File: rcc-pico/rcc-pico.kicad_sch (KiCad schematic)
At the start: 51 parts, among them J1 Conn_02x02_Odd_Even, J10 Conn_02x04_Odd_Even, J11 Conn_02x04_Odd_Even, J12 Conn_02x04_Odd_Even, J14 Conn_02x05_Odd_Even, J16 Conn_01x02_Pin, J3 PJ-006A, J5 Conn_3x4_female, J7 Conn_03x10, J8 Screw_Terminal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

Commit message: fixed D2 footprint
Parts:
- D2: footprint LED_SMD:LED_0603_1608Metric_Pad1.05x0.95mm_HandSolder -> LED_SMD:LED_0603_1608Metric
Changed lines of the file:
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@@
       (effects (font (size 1.27 1.27)))
     )
-    (property "Footprint" "LED_SMD:LED_0603_1608Metric_Pad1.05x0.95mm_HandSolder" (at 60.96 124.46 0)
+    (property "Footprint" "LED_SMD:LED_0603_1608Metric" (at 60.96 124.46 0)
       (effects (font (size 1.27 1.27)) hide)
     )

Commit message: final touches, fixed footprints
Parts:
- R10, R5, R6, R7, R8, R9: footprint Resistor_SMD:R_0603_1608Metric_Pad0.98x0.95mm_HandSolder -> Resistor_SMD:R_0603_1608Metric
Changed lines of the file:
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@@
       (effects (font (size 1.27 1.27)) (justify left))
     )
-    (property "Footprint" "Resistor_SMD:R_0603_1608Metric_Pad0.98x0.95mm_HandSolder" (at 94.996 170.434 90)
+    (property "Footprint" "Resistor_SMD:R_0603_1608Metric" (at 94.996 170.434 90)
       (effects (font (size 1.27 1.27)) hide)
     )
@@
       (effects (font (size 1.27 1.27)) (justify left))
     )
-    (property "Footprint" "Resistor_SMD:R_0603_1608Metric_Pad0.98x0.95mm_HandSolder" (at 65.786 170.434 90)
+    (property "Footprint" "Resistor_SMD:R_0603_1608Metric" (at 65.786 170.434 90)
       (effects (font (size 1.27 1.27)) hide)
     )
@@
       (effects (font (size 1.27 1.27)) (justify left))
     )
-    (property "Footprint" "Resistor_SMD:R_0603_1608Metric_Pad0.98x0.95mm_HandSolder" (at 50.546 170.434 90)
+    (property "Footprint" "Resistor_SMD:R_0603_1608Metric" (at 50.546 170.434 90)
       (effects (font (size 1.27 1.27)) hide)
     )
@@
       (effects (font (size 1.27 1.27)) (justify left))
     )
-    (property "Footprint" "Resistor_SMD:R_0603_1608Metric_Pad0.98x0.95mm_HandSolder" (at 36.576 170.434 90)
+    (property "Footprint" "Resistor_SMD:R_0603_1608Metric" (at 36.576 170.434 90)
       (effects (font (size 1.27 1.27)) hide)
     )
@@
       (effects (font (size 1.27 1.27)) (justify left))
     )
-    (property "Footprint" "Resistor_SMD:R_0603_1608Metric_Pad0.98x0.95mm_HandSolder" (at 21.336 170.434 90)
+    (property "Footprint" "Resistor_SMD:R_0603_1608Metric" (at 21.336 170.434 90)
       (effects (font (size 1.27 1.27)) hide)
     )
@@
       (effects (font (size 1.27 1.27)) (justify left))
     )
-    (property "Footprint" "Resistor_SMD:R_0603_1608Metric_Pad0.98x0.95mm_HandSolder" (at 79.756 170.434 90)
-      (effects (font (size 1.27 1.27)) hide)
-    )
+    (property "Footprint" "Resistor_SMD:R_0603_1608Metric" (at 79.756 170.434 90)
+      (effects (font (size 1.27 1.27)) hide)
+    )

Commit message: changed 0.1uH footprint, added v0.2 BOM
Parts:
- C1, C7: footprint Capacitor_SMD:C_0603_1608Metric -> Capacitor_SMD:C_0402_1005Metric
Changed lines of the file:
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@@
       (effects (font (size 1.27 1.27)))
     )
-    (property "Footprint" "Capacitor_SMD:C_0603_1608Metric" (at 138.43 32.0548 0)
+    (property "Footprint" "Capacitor_SMD:C_0402_1005Metric" (at 138.43 32.0548 0)
       (effects (font (size 1.27 1.27)) hide)
     )
@@
       (effects (font (size 1.27 1.27)))
     )
-    (property "Footprint" "Capacitor_SMD:C_0603_1608Metric" (at 210.5152 78.74 0)
+    (property "Footprint" "Capacitor_SMD:C_0402_1005Metric" (at 210.5152 78.74 0)
       (effects (font (size 1.27 1.27)) hide)
     )

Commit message: ordering v0.2
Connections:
- net GND: no longer H1.1, H2.1, H3.1, H4.1
- net GPIO26: now also J4.25 (5); no longer J4.3 (Pin_3)
- net GPIO27: now also J4.26 (6); no longer J4.25 (5)
- net GPIO28: now also J4.3 (Pin_3); no longer J4.26 (6)
- no-connect marks 16 -> 20
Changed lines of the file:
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@@
   (no_connect (at 256.54 22.86))
   (no_connect (at 276.86 20.32))
+  (no_connect (at 191.77 48.26))
   (no_connect (at 203.2 86.36))
   (no_connect (at 276.86 22.86))
@@
   (no_connect (at 243.84 22.86))
   (no_connect (at 187.96 132.08))
+  (no_connect (at 191.77 31.75))
   (no_connect (at 264.16 22.86))
+  (no_connect (at 191.77 39.37))
   (no_connect (at 203.2 78.74))
   (no_connect (at 203.2 88.9))
   (no_connect (at 276.86 25.4))
   (no_connect (at 264.16 20.32))
+  (no_connect (at 191.77 55.88))
   (no_connect (at 182.88 132.08))
   (wire (pts (xy 30.48 43.18) (xy 33.02 43.18))
@@
     (effects (font (size 1.27 1.27)) (justify right bottom))
   )
+  (label "GPIO28" (at 234.95 78.74 0) (fields_autoplaced)
+    (effects (font (size 1.27 1.27)) (justify left bottom))
+  )
   (label "GPIO27" (at 203.2 99.06 0) (fields_autoplaced)
     (effects (font (size 1.27 1.27)) (justify left bottom))
@@
     (effects (font (size 1.27 1.27)) (justify right bottom))
   )
+  (label "GPIO26" (at 254 83.82 0) (fields_autoplaced)
+    (effects (font (size 1.27 1.27)) (justify left bottom))
+  )
   (label "GND" (at 167.64 121.92 180) (fields_autoplaced)
     (effects (font (size 1.27 1.27)) (justify right bottom))
@@
     (effects (font (size 1.27 1.27)) (justify right bottom))
   )
-  (label "GND" (at 191.77 48.26 0) (fields_autoplaced)
-    (effects (font (size 1.27 1.27)) (justify left bottom))
-  )
   (label "GPIO10" (at 130.81 113.03 180) (fields_autoplaced)
     (effects (font (size 1.27 1.27)) (justify right bottom))
   )
-  (label "GND" (at 191.77 31.75 0) (fields_autoplaced)
-    (effects (font (size 1.27 1.27)) (justify left bottom))
-  )
   (label "GND" (at 203.2 83.82 0) (fields_autoplaced)
     (effects (font (size 1.27 1.27)) (justify left bottom))
@@
     (effects (font (size 1.27 1.27)) (justify right bottom))
   )
-  (label "GPIO27" (at 254 83.82 0) (fields_autoplaced)
-    (effects (font (size 1.27 1.27)) (justify left bottom))
-  )
   (label "GPIO14" (at 167.64 124.46 180) (fields_autoplaced)
     (effects (font (size 1.27 1.27)) (justify right bottom))
@@
     (effects (font (size 1.27 1.27)) (justify right bottom))
   )
-  (label "GND" (at 191.77 55.88 0) (fields_autoplaced)
-    (effects (font (size 1.27 1.27)) (justify left bottom))
-  )
-  (label "GPIO28" (at 254 86.36 0) (fields_autoplaced)
-    (effects (font (size 1.27 1.27)) (justify left bottom))
-  )
   (label "adcref_3v3" (at 265.43 54.61 0) (fields_autoplaced)
     (effects (font (size 1.27 1.27)) (justify left bottom))
@@
     (effects (font (size 1.27 1.27)) (justify left bottom))
   )
-  (label "GND" (at 191.77 39.37 0) (fields_autoplaced)
-    (effects (font (size 1.27 1.27)) (justify left bottom))
-  )
   (label "GND" (at 203.2 109.22 0) (fields_autoplaced)
     (effects (font (size 1.27 1.27)) (justify left bottom))
@@
     (effects (font (size 1.27 1.27)) (justify right bottom))
   )
-  (label "GPIO26" (at 234.95 78.74 0) (fields_autoplaced)
-    (effects (font (size 1.27 1.27)) (justify left bottom))
-  )
   (label "GND" (at 203.2 121.92 0) (fields_autoplaced)
     (effects (font (size 1.27 1.27)) (justify left bottom))
@@
     (effects (font (size 1.27 1.27)) (justify right bottom))
   )
+  (label "GPIO27" (at 254 86.36 0) (fields_autoplaced)
+    (effects (font (size 1.27 1.27)) (justify left bottom))
+  )
   (label "GPIO19" (at 252.73 124.46 0) (fields_autoplaced)

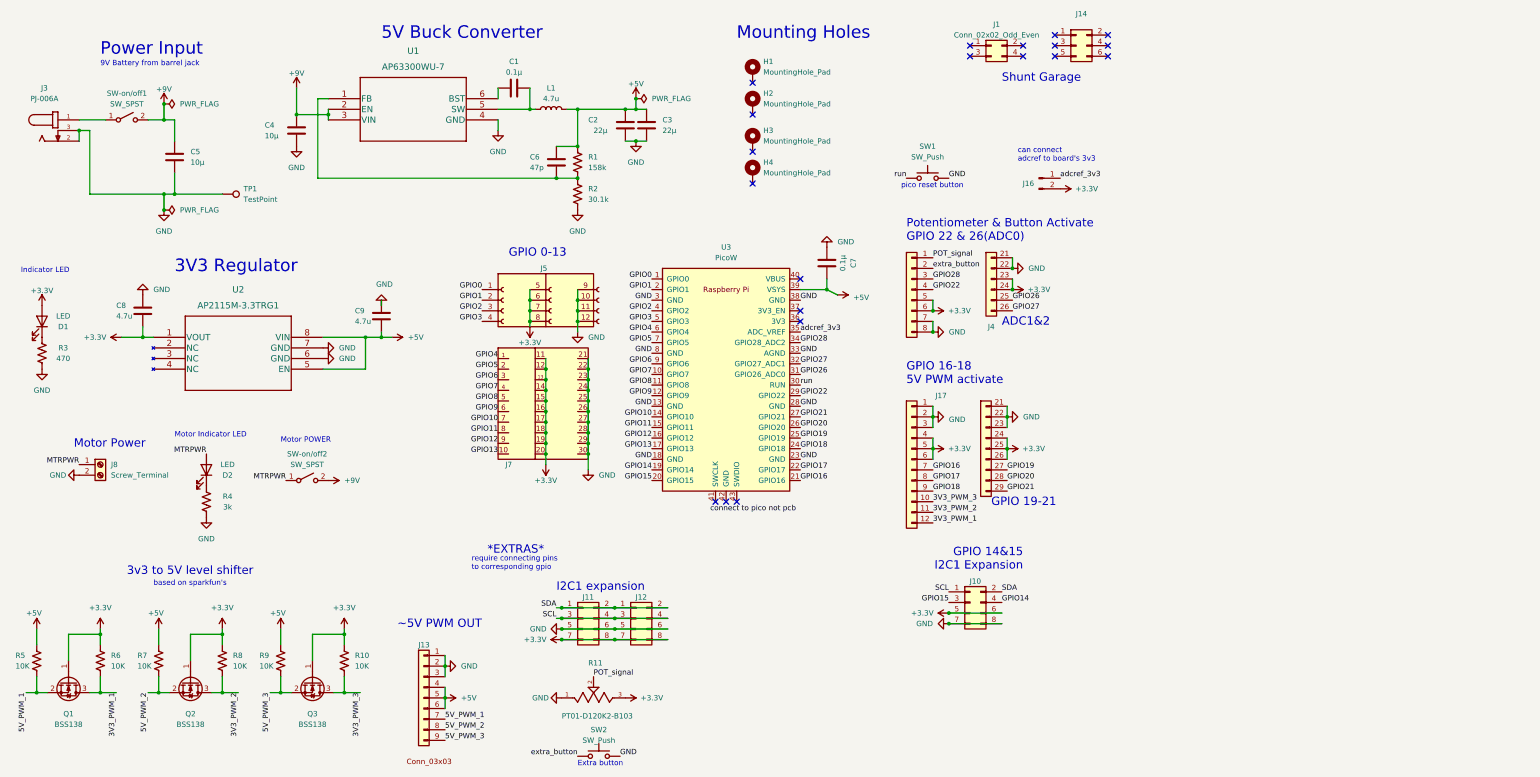
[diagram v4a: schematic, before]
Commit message: v0.3 modifications, added input protection diode
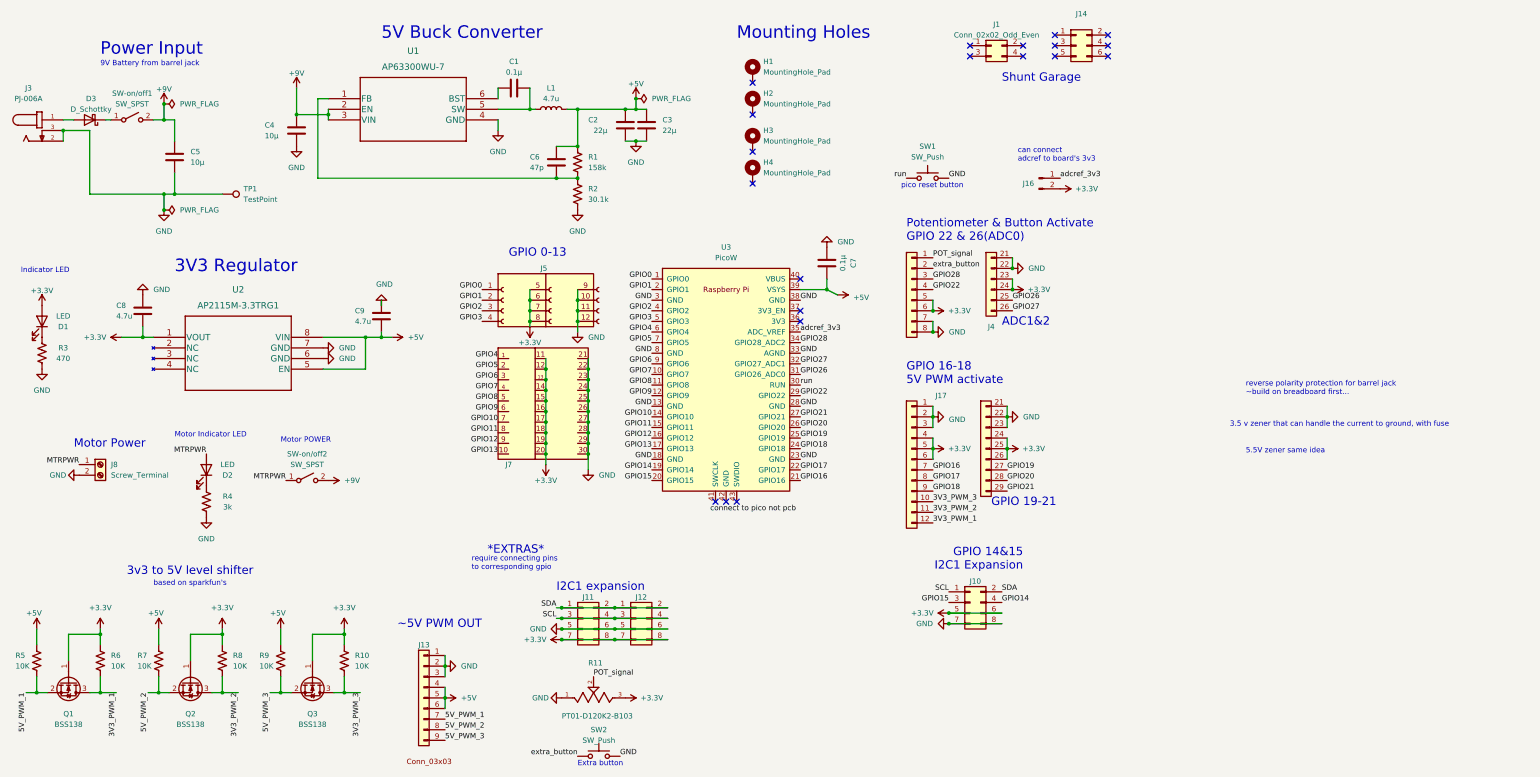
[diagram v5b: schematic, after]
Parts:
- added D3: D_Schottky, custom-components:DIOM5227X270N, symbol Device:D_Schottky
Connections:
- net at SW-on/off1.1 (A): now also D3.1 (K); no longer J3.1
- new net: D3.2 (A), J3.1
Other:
- note added: "3.5 v zener that can handle the current to ground, with fuse"
- note added: "5.5V zener same idea"
- note added: "reverse polarity protection for barrel jack ~build on breadboard first..."
- moved on the sheet: J3, SW-on/off1
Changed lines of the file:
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@@
   (junction (at 209.55 81.28) (diameter 0) (color 0 0 0 0)
   )
-  (junction (at 30.48 43.18) (diameter 0) (color 0 0 0 0)
+  (junction (at 26.67 43.18) (diameter 0) (color 0 0 0 0)
   )
   (junction (at 158.75 165.1) (diameter 0) (color 0 0 0 0)
@@
   (no_connect (at 191.77 55.88))
   (no_connect (at 182.88 132.08))
-  (wire (pts (xy 30.48 43.18) (xy 33.02 43.18))
+  (wire (pts (xy 26.67 43.18) (xy 33.02 43.18))
     (stroke (width 0) (type default))
   )
@@
     (stroke (width 0) (type default))
   )
-  (wire (pts (xy 30.48 40.64) (xy 36.83 40.64))
-    (stroke (width 0) (type default))
-  )
   (wire (pts (xy 158.75 157.48) (xy 171.45 157.48))
     (stroke (width 0) (type default))
@@
     (stroke (width 0) (type default))
   )
+  (wire (pts (xy 33.02 43.18) (xy 33.02 58.42))
+    (stroke (width 0) (type default))
+  )
   (wire (pts (xy 17.78 177.8) (xy 20.32 177.8))
     (stroke (width 0) (type default))
@@
     (stroke (width 0) (type default))
   )
-  (wire (pts (xy 33.02 43.18) (xy 33.02 58.42))
-    (stroke (width 0) (type default))
-  )
   (wire (pts (xy 138.43 86.36) (xy 138.43 88.9))
     (stroke (width 0) (type default))
@@
     (stroke (width 0) (type default))
   )
-  (wire (pts (xy 30.48 43.18) (xy 30.48 45.72))
+  (wire (pts (xy 26.67 43.18) (xy 26.67 45.72))
     (stroke (width 0) (type default))
   )
@@
     (stroke (width 0) (type default))
   )
+  (wire (pts (xy 38.1 40.64) (xy 36.83 40.64))
+    (stroke (width 0) (type default))
+  )
   (wire (pts (xy 90.17 39.37) (xy 90.17 40.64))
     (stroke (width 0) (type default))
@@
     (stroke (width 0) (type default))
   )
-  (wire (pts (xy 46.99 40.64) (xy 50.8 40.64))
+  (wire (pts (xy 48.26 40.64) (xy 50.8 40.64))
     (stroke (width 0) (type default))
   )
@@
     (stroke (width 0) (type default))
   )
+  (wire (pts (xy 26.67 40.64) (xy 29.21 40.64))
+    (stroke (width 0) (type default))
+  )
   (wire (pts (xy 238.76 161.29) (xy 251.46 161.29))
     (stroke (width 0) (type default))
@@
   )
   (text "require connecting pins\nto corresponding gpio" (at 124.46 148.59 0)
+    (effects (font (size 1.27 1.27)) (justify left bottom))
+  )
+  (text "5.5V zener same idea" (at 309.88 120.65 0)
     (effects (font (size 1.27 1.27)) (justify left bottom))
   )
@@
   (text "I2C1 expansion" (at 144.78 153.67 0)
     (effects (font (size 2 2)) (justify left bottom))
+  )
+  (text "reverse polarity protection for barrel jack\n~build on breadboard first..."
+    (at 309.88 106.68 0)
+    (effects (font (size 1.27 1.27)) (justify left bottom))
   )
   (text "3V3 Regulator" (at 53.34 77.47 0)
@@
   )
   (text "9V Battery from barrel jack" (at 35.56 27.94 0)
+    (effects (font (size 1.27 1.27)) (justify left bottom))
+  )
+  (text "3.5 v zener that can handle the current to ground, with fuse"
+    (at 306.07 114.3 0)
     (effects (font (size 1.27 1.27)) (justify left bottom))
   )
@@
     )
   )
-  (symbol (lib_id "Switch:SW_SPST") (at 41.91 40.64 0) (unit 1)
-    (in_bom yes) (on_board yes) (dnp no) (fields_autoplaced)
-    (property "Reference" "SW-on/off1" (at 41.91 34.29 0)
-      (effects (font (size 1.27 1.27)))
-    )
-    (property "Value" "SW_SPST" (at 41.91 36.83 0)
-      (effects (font (size 1.27 1.27)))
-    )
-    (property "Footprint" "PicoShieldHeaders:SW_OS102011MS2QN1" (at 41.91 40.64 0)
-      (effects (font (size 1.27 1.27)) hide)
-    )
-    (property "Datasheet" "~" (at 41.91 40.64 0)
-      (effects (font (size 1.27 1.27)) hide)
-    )
-    (property "Field4" "" (at 41.91 40.64 0)
+  (symbol (lib_id "Switch:SW_SPST") (at 43.18 40.64 0) (unit 1)
+    (in_bom yes) (on_board yes) (dnp no) (fields_autoplaced)
+    (property "Reference" "SW-on/off1" (at 43.18 34.29 0)
+      (effects (font (size 1.27 1.27)))
+    )
+    (property "Value" "SW_SPST" (at 43.18 36.83 0)
+      (effects (font (size 1.27 1.27)))
+    )
+    (property "Footprint" "PicoShieldHeaders:SW_OS102011MS2QN1" (at 43.18 40.64 0)
+      (effects (font (size 1.27 1.27)) hide)
+    )
+    (property "Datasheet" "~" (at 43.18 40.64 0)
+      (effects (font (size 1.27 1.27)) hide)
+    )
+    (property "Field4" "" (at 43.18 40.64 0)
       (effects (font (size 1.27 1.27)) hide)
     )
@@
     )
   )
-  (symbol (lib_id "power:PJ-006A") (at 25.4 43.18 0) (unit 1)
-    (in_bom yes) (on_board yes) (dnp no) (fields_autoplaced)
-    (property "Reference" "J3" (at 22.1615 33.02 0)
-      (effects (font (size 1.27 1.27)))
-    )
-    (property "Value" "PJ-006A" (at 22.1615 35.56 0)
-      (effects (font (size 1.27 1.27)))
-    )
-    (property "Footprint" "PicoShieldHeaders:CUI_PJ-006A" (at 25.4 43.18 0)
+  (symbol (lib_id "power:PJ-006A") (at 21.59 43.18 0) (unit 1)
+    (in_bom yes) (on_board yes) (dnp no) (fields_autoplaced)
+    (property "Reference" "J3" (at 18.3515 33.02 0)
+      (effects (font (size 1.27 1.27)))
+    )
+    (property "Value" "PJ-006A" (at 18.3515 35.56 0)
+      (effects (font (size 1.27 1.27)))
+    )
+    (property "Footprint" "PicoShieldHeaders:CUI_PJ-006A" (at 21.59 43.18 0)
       (effects (font (size 1.27 1.27)) (justify left bottom) hide)
     )
-    (property "Datasheet" "" (at 25.4 43.18 0)
+    (property "Datasheet" "" (at 21.59 43.18 0)
       (effects (font (size 1.27 1.27)) (justify left bottom) hide)
     )
-    (property "STANDARD" "Manufacturer recommendations" (at 25.4 43.18 0)
+    (property "STANDARD" "Manufacturer recommendations" (at 21.59 43.18 0)
       (effects (font (size 1.27 1.27)) (justify left bottom) hide)
     )
-    (property "MANUFACTURER" "CUI INC" (at 25.4 43.18 0)
+    (property "MANUFACTURER" "CUI INC" (at 21.59 43.18 0)
       (effects (font (size 1.27 1.27)) (justify left bottom) hide)
     )
@@
         )
       )
+    )
+  )
+  (symbol (lib_id "Device:D_Schottky") (at 33.02 40.64 180) (unit 1)
+    (in_bom yes) (on_board yes) (dnp no) (fields_autoplaced)
+    (property "Reference" "D3" (at 33.3375 35.56 0)
+      (effects (font (size 1.27 1.27)))
+    )
+    (property "Value" "D_Schottky" (at 33.3375 38.1 0)
+      (effects (font (size 1.27 1.27)))
+    )
+    (property "Footprint" "custom-components:DIOM5227X270N" (at 33.02 40.64 0)
+      (effects (font (size 1.27 1.27)) hide)
+    )
+    (property "Datasheet" "~" (at 33.02 40.64 0)
+      (effects (font (size 1.27 1.27)) hide)
+    )
+    (pin "1")
+    (pin "2")
+    (instances
+      (project "rcc-pico"
+        (path "/58206809-86e0-49ef-aaca-4b88089e8130"
+          (reference "D3") (unit 1)
+        )
+      )
